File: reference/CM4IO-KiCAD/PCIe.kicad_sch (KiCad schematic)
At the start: 24 parts

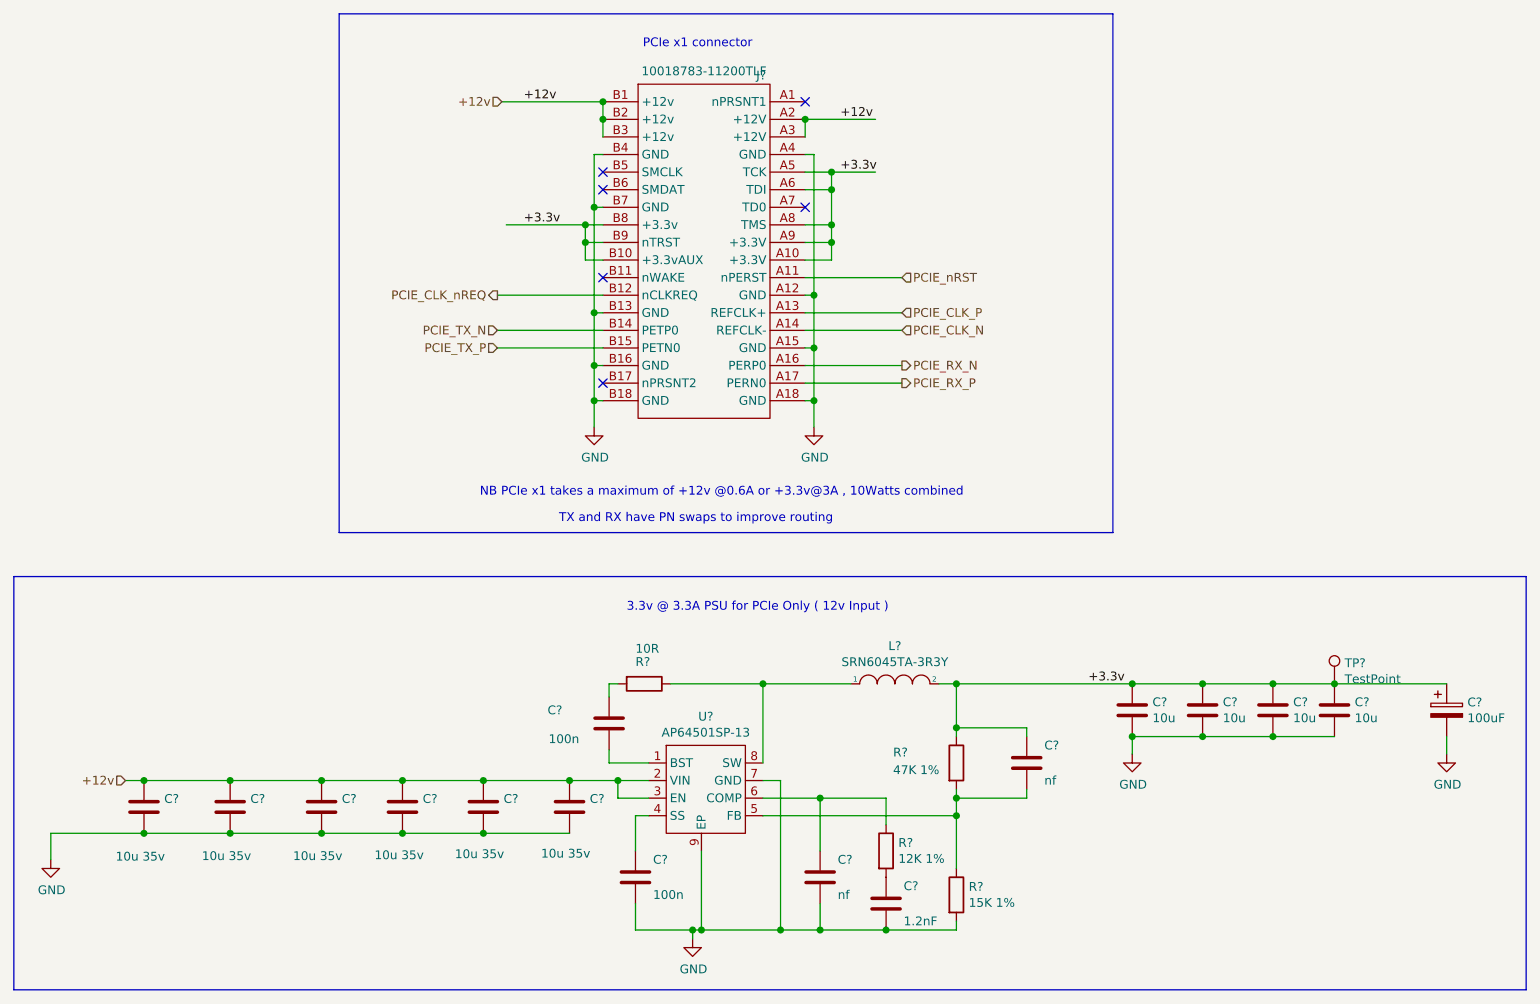
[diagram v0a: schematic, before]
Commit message: start routing mezzanine
making a progress capture before trying to cram a lot of signals onto just one hirose connector...
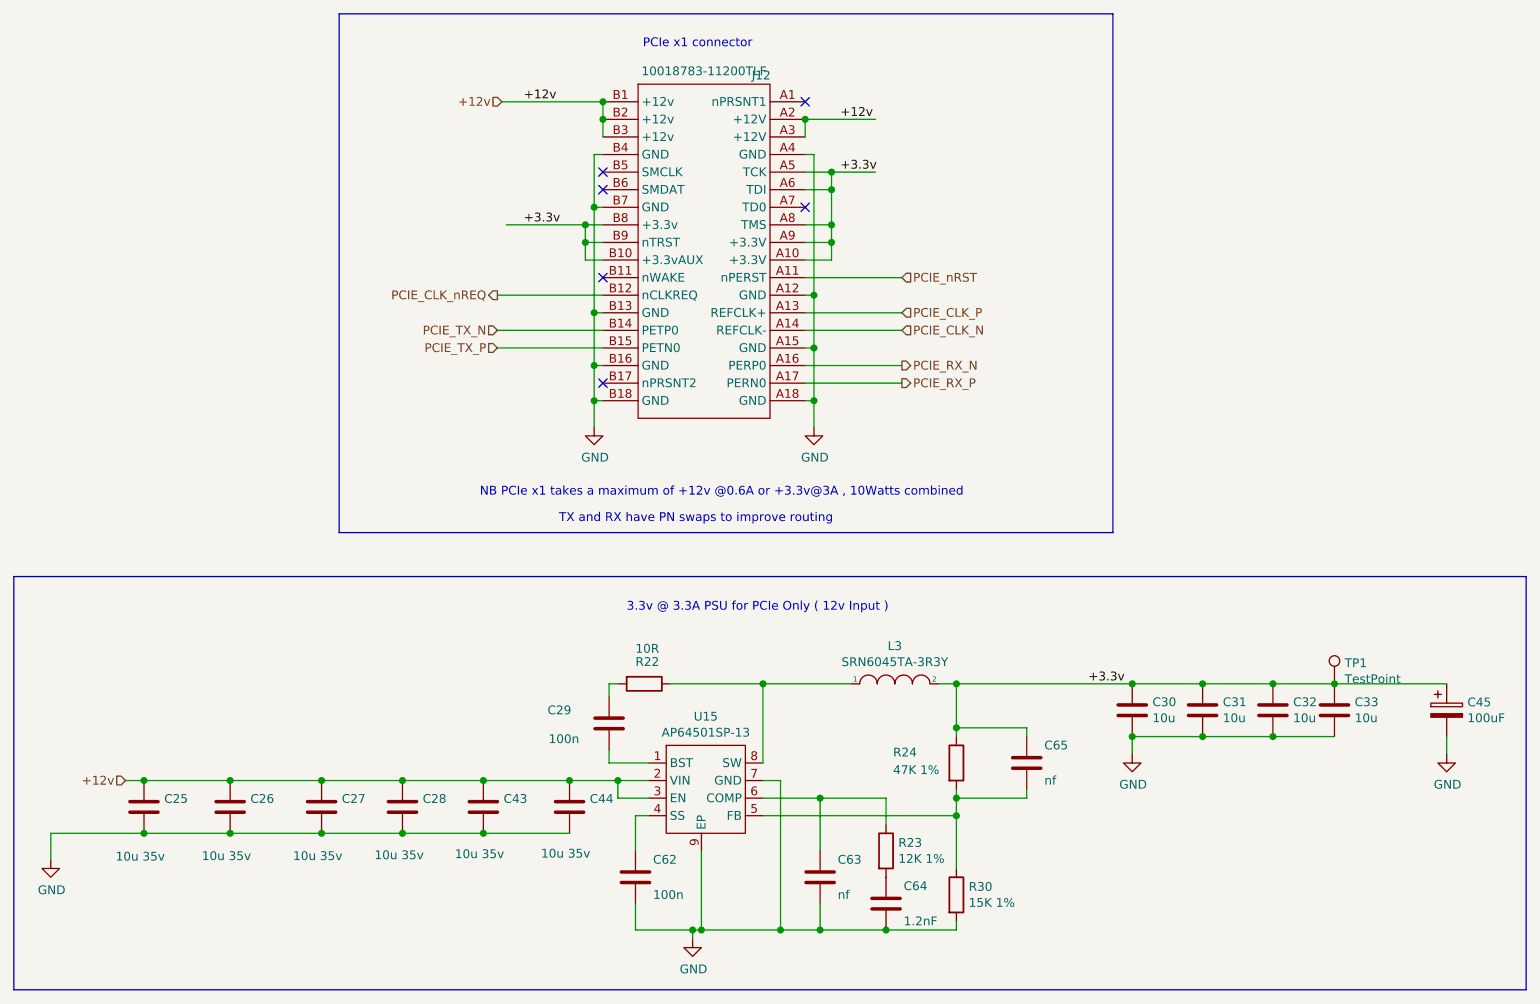
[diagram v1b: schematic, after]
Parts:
- gave numbers to parts that had none: 24
